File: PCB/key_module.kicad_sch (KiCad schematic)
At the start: 1 part

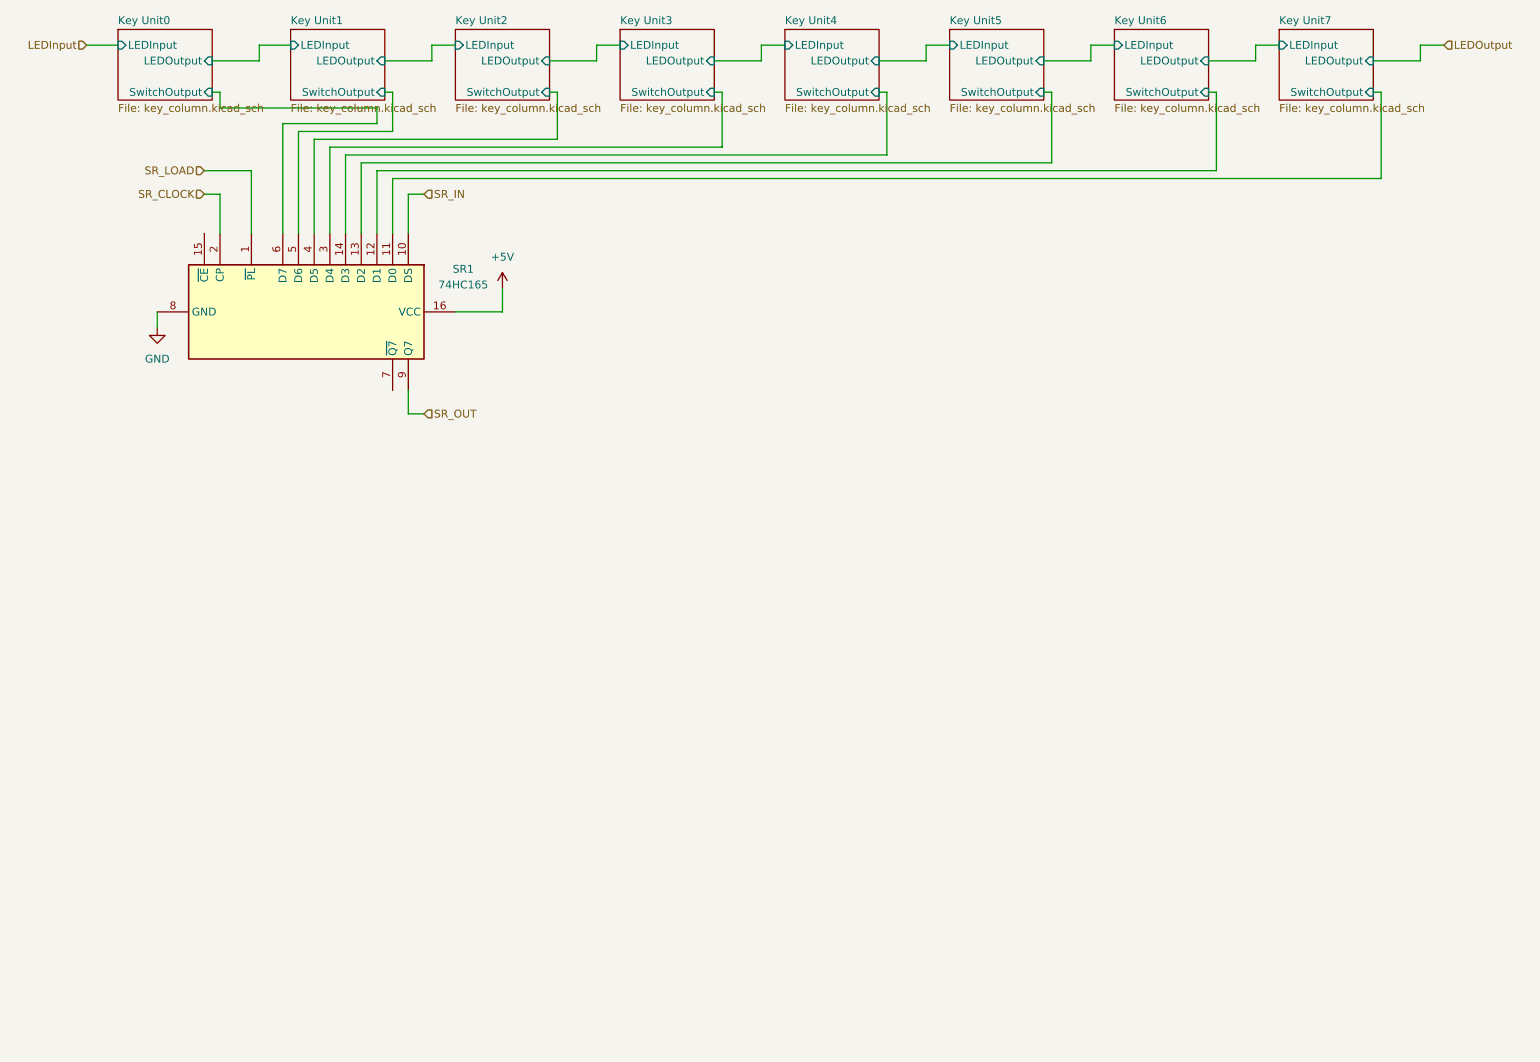
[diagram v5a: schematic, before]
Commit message: Removed 8-key units, now using the PCB view to handle routing the keys to the SOIP shift registers.
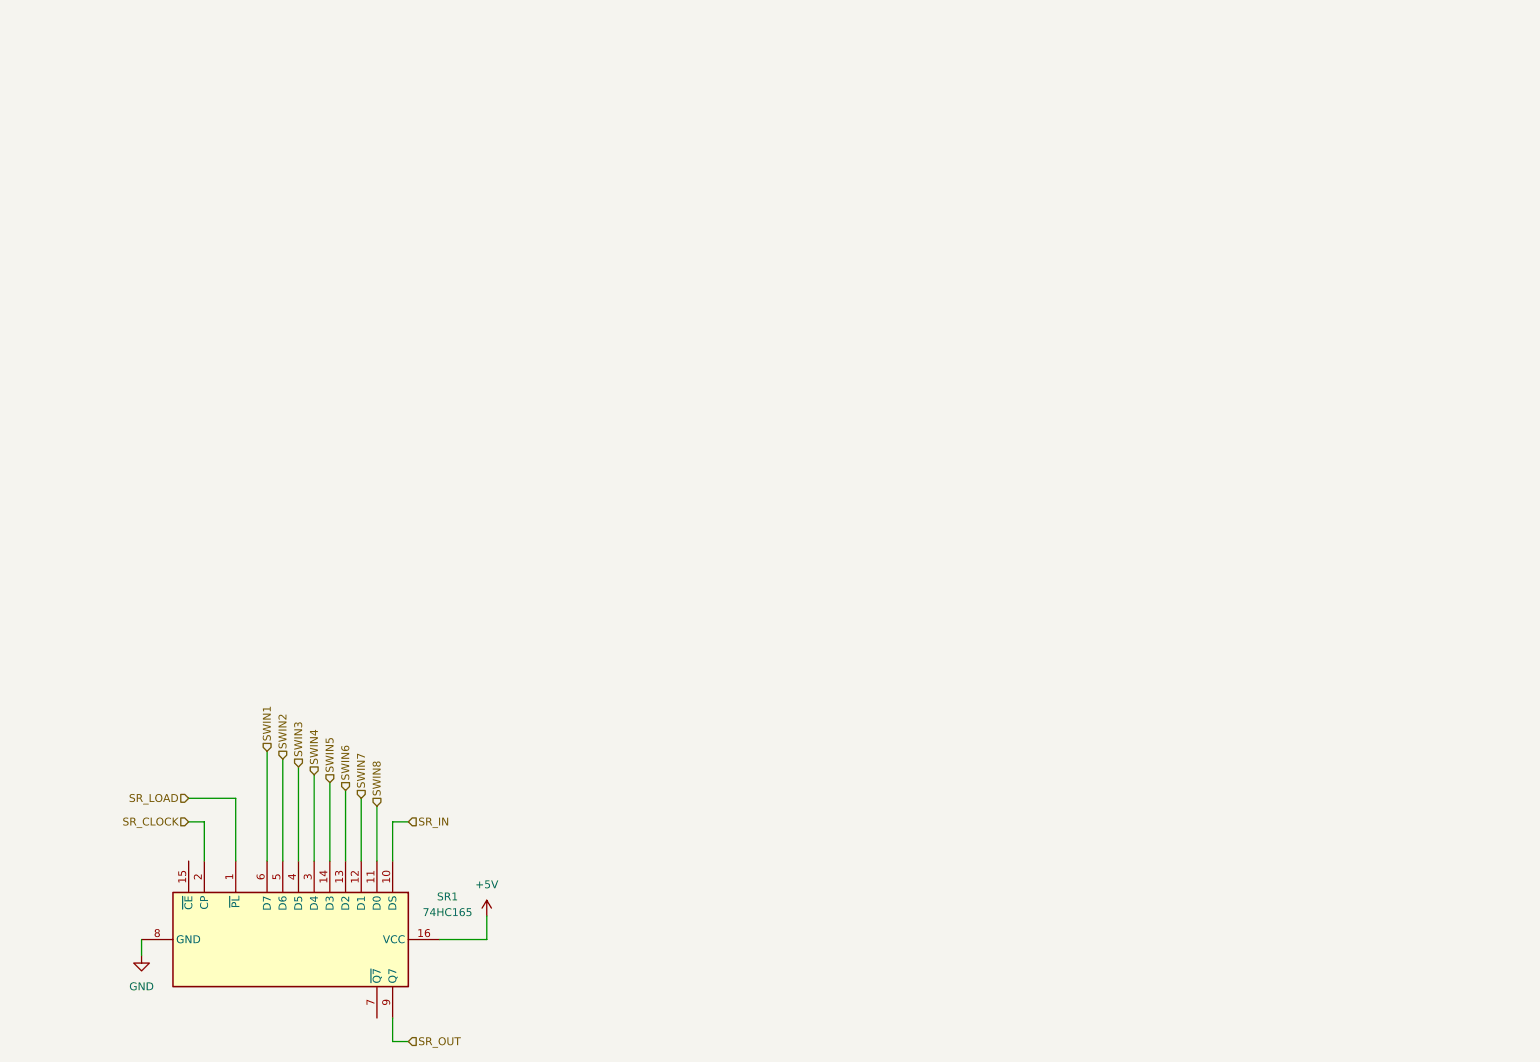
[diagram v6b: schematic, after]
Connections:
- net Key Unit0/SwitchOutput renamed SWIN1
- net Key Unit1/SwitchOutput renamed SWIN2
- net Key Unit2/SwitchOutput renamed SWIN3
- net Key Unit3/SwitchOutput renamed SWIN4
- net Key Unit4/SwitchOutput renamed SWIN5
- net Key Unit5/SwitchOutput renamed SWIN6
- net Key Unit6/SwitchOutput renamed SWIN7
- net Key Unit7/SwitchOutput renamed SWIN8
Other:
- removed sheet Key Unit0
- removed sheet Key Unit1
- removed sheet Key Unit2
- removed sheet Key Unit3
- removed sheet Key Unit4
- removed sheet Key Unit5
- removed sheet Key Unit6
- removed sheet Key Unit7
- moved on the sheet: SR1

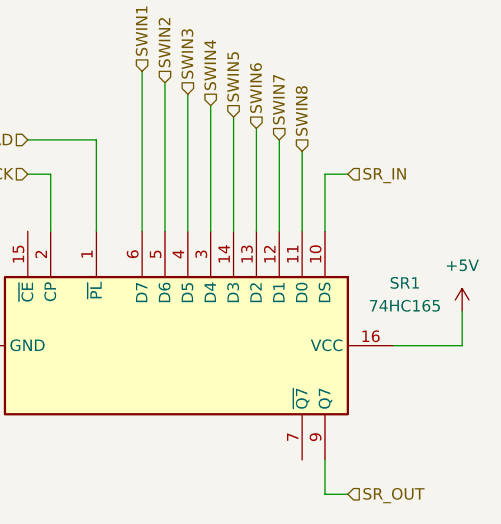
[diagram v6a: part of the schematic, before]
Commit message: Updated schematics for KiCAD 8
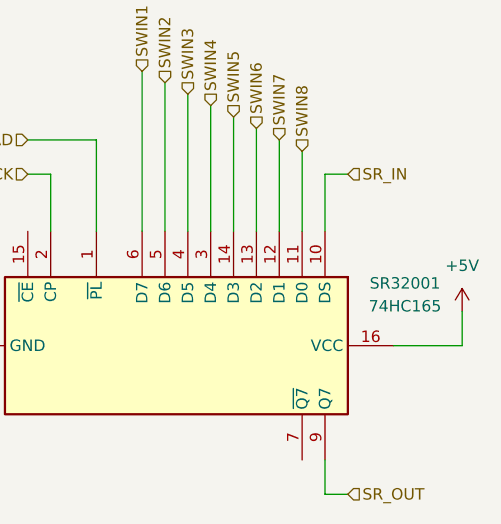
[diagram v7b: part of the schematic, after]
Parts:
- renumbered SR1 to SR32001
